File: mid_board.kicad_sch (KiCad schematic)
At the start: 21 parts, among them J4 Conn_01x10_Pin, J5 Conn_01x02_Pin, J6 Conn_01x11_Pin, J7 Conn_01x07_Pin, J8 Conn_01x08_Pin, J9 Conn_01x06_Pin, U2 Z80CPU, U3 74LS374, U4 74ALS00, U5 74ALS32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

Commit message: Added some basic traces for power
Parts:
- removed C1, C2, C3, C4, C5: C_Small, symbol Device:C_Small
- removed J4: Conn_01x10_Pin, symbol Connector:Conn_01x10_Pin
- removed J5: Conn_01x02_Pin, symbol Connector:Conn_01x02_Pin
- removed J6: Conn_01x11_Pin, symbol Connector:Conn_01x11_Pin
- removed J7: Conn_01x07_Pin, symbol Connector:Conn_01x07_Pin
- removed J8: Conn_01x08_Pin, symbol Connector:Conn_01x08_Pin
- removed J9: Conn_01x06_Pin, symbol Connector:Conn_01x06_Pin
- removed U8, U9: 74LS83, symbol 74xx:74LS83
- added U20, U8: 74LS283, Package_SO:SOIC-16_3.9x9.9mm_P1.27mm, symbol 74xx:74LS283
- R1, R2: footprint (none) -> Resistor_SMD:R_1206_3216Metric_Pad1.30x1.75mm_HandSolder
- U2: footprint (none) -> Package_DIP:DIP-40_W15.24mm_Socket
- U3, U6, U7: footprint (none) -> Package_SO:SO-20_5.3x12.6mm_P1.27mm
- U4, U5: footprint (none) -> Package_SO:SOIC-14_3.9x8.7mm_P1.27mm
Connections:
- net A0: now also U8.11 (B4)
- net A1: now also U20.11 (B4)
- net A2: now also U8.15 (B3)
- net A3: now also U20.15 (B3)
- net A4: now also U8.2 (B2)
- net A5: now also U20.2 (B2)
- net A6: now also U8.6 (B1)
- net A7: now also U20.6 (B1)
- net BUF_D0: now also U8.12 (A4)
- net BUF_D1: now also U8.14 (A3)
- net BUF_D2: now also U8.3 (A2)
- net BUF_D3: now also U8.5 (A1)
- net BUF_D4: now also U20.12 (A4)
- net BUF_D5: now also U20.14 (A3)
- net BUF_D6: now also U20.3 (A2)
- net BUF_D7: now also U20.5 (A1)
- net GND: now also U4.1, U4.12, U4.13, U4.2, U20.8 (GND), U8.7 (C0), U8.8 (GND)
- net VCC: now also U20.16 (VCC), U8.16 (VCC)
- net at U7.11 (I0b): now also U20.4 (S1)
- net at U7.13 (I1b): now also U20.1 (S2)
- net at U7.15 (I2b): now also U20.13 (S3)
- net at U7.17 (I3b): now also U20.10 (S4)
- net at U7.2 (I0a): now also U8.4 (S1)
- net at U7.4 (I1a): now also U8.1 (S2)
- net at U7.6 (I2a): now also U8.13 (S3)
- net at U7.8 (I3a): now also U8.10 (S4)
- new net: U20.7 (C0), U8.9 (C4)
- no-connect marks 7 -> 3
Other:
- moved on the sheet: U4E, U5E

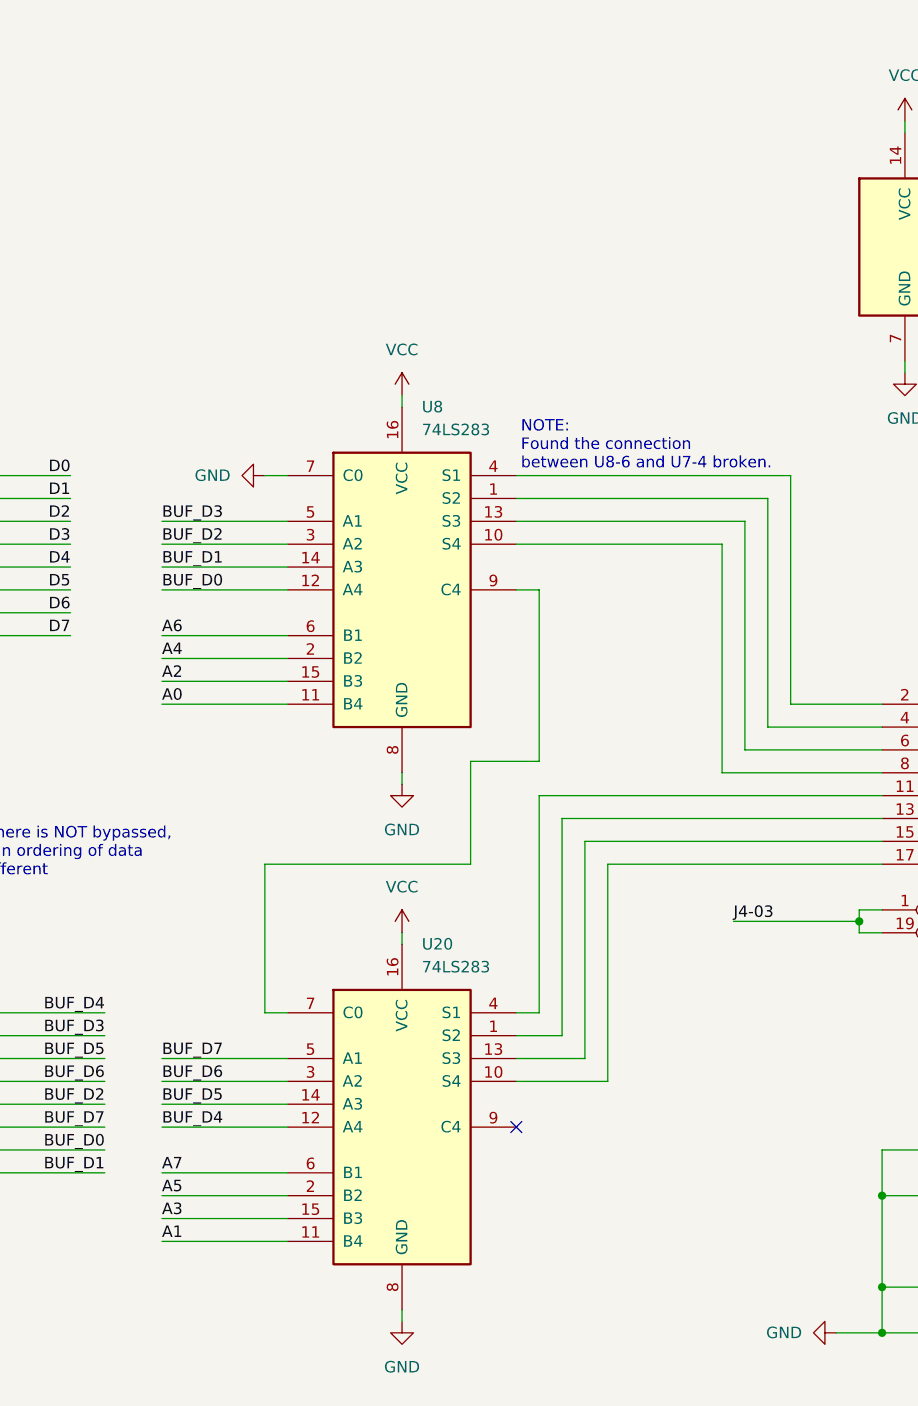
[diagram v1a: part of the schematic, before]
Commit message: Fix adder bit ordering
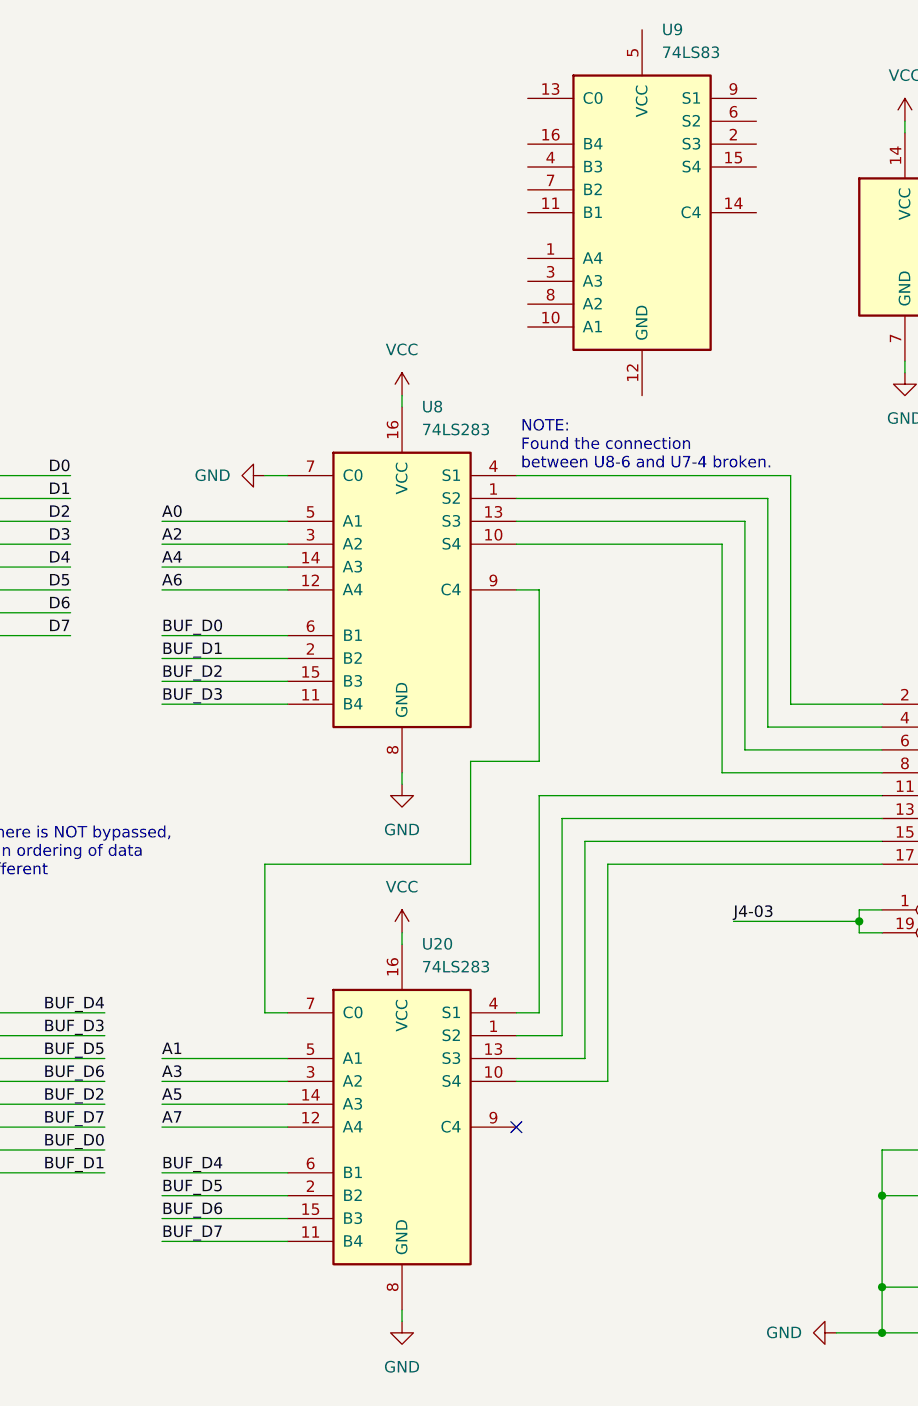
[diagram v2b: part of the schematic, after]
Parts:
- added U9: 74LS83, symbol 74xx:74LS83
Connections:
- net A0: now also U8.5 (A1); no longer U8.11 (B4)
- net A1: now also U20.5 (A1); no longer U20.11 (B4)
- net A2: now also U8.3 (A2); no longer U8.15 (B3)
- net A3: now also U20.3 (A2); no longer U20.15 (B3)
- net A4: now also U8.14 (A3); no longer U8.2 (B2)
- net A5: now also U20.14 (A3); no longer U20.2 (B2)
- net A6: now also U8.12 (A4); no longer U8.6 (B1)
- net A7: now also U20.12 (A4); no longer U20.6 (B1)
- net BUF_D0: now also U8.6 (B1); no longer U8.12 (A4)
- net BUF_D1: now also U8.2 (B2); no longer U8.14 (A3)
- net BUF_D2: now also U8.15 (B3); no longer U8.3 (A2)
- net BUF_D3: now also U8.11 (B4); no longer U8.5 (A1)
- net BUF_D4: now also U20.6 (B1); no longer U20.12 (A4)
- net BUF_D5: now also U20.2 (B2); no longer U20.14 (A3)
- net BUF_D6: now also U20.15 (B3); no longer U20.3 (A2)
- net BUF_D7: now also U20.11 (B4); no longer U20.5 (A1)
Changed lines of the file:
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@@
 	(wire
 		(pts
-			(xy 153.67 134.62) (xy 167.64 134.62)
+			(xy 153.67 144.78) (xy 167.64 144.78)
 		)
 		(stroke
@@
 	(wire
 		(pts
-			(xy 153.67 77.47) (xy 167.64 77.47)
+			(xy 153.67 82.55) (xy 167.64 82.55)
 		)
 		(stroke
@@
 	(wire
 		(pts
-			(xy 153.67 90.17) (xy 167.64 90.17)
+			(xy 153.67 69.85) (xy 167.64 69.85)
 		)
 		(stroke
@@
 	(wire
 		(pts
-			(xy 153.67 87.63) (xy 167.64 87.63)
+			(xy 153.67 72.39) (xy 167.64 72.39)
 		)
 		(stroke
@@
 	(wire
 		(pts
-			(xy 153.67 69.85) (xy 167.64 69.85)
+			(xy 153.67 90.17) (xy 167.64 90.17)
 		)
 		(stroke
@@
 	(wire
 		(pts
-			(xy 153.67 147.32) (xy 167.64 147.32)
+			(xy 153.67 132.08) (xy 167.64 132.08)
 		)
 		(stroke
@@
 	(wire
 		(pts
-			(xy 153.67 72.39) (xy 167.64 72.39)
+			(xy 153.67 87.63) (xy 167.64 87.63)
 		)
 		(stroke
@@
 	(wire
 		(pts
-			(xy 153.67 132.08) (xy 167.64 132.08)
+			(xy 153.67 147.32) (xy 167.64 147.32)
 		)
 		(stroke
@@
 	(wire
 		(pts
-			(xy 153.67 74.93) (xy 167.64 74.93)
+			(xy 153.67 85.09) (xy 167.64 85.09)
 		)
 		(stroke
@@
 	(wire
 		(pts
-			(xy 153.67 137.16) (xy 167.64 137.16)
+			(xy 153.67 142.24) (xy 167.64 142.24)
 		)
 		(stroke
@@
 	(wire
 		(pts
-			(xy 153.67 149.86) (xy 167.64 149.86)
+			(xy 153.67 129.54) (xy 167.64 129.54)
 		)
 		(stroke
@@
 	(wire
 		(pts
-			(xy 153.67 142.24) (xy 167.64 142.24)
+			(xy 153.67 137.16) (xy 167.64 137.16)
 		)
 		(stroke
@@
 	(wire
 		(pts
-			(xy 153.67 129.54) (xy 167.64 129.54)
+			(xy 153.67 149.86) (xy 167.64 149.86)
 		)
 		(stroke
@@
 	(wire
 		(pts
-			(xy 153.67 85.09) (xy 167.64 85.09)
+			(xy 153.67 74.93) (xy 167.64 74.93)
 		)
 		(stroke
@@
 	(wire
 		(pts
-			(xy 153.67 82.55) (xy 167.64 82.55)
+			(xy 153.67 77.47) (xy 167.64 77.47)
 		)
 		(stroke
@@
 	(wire
 		(pts
-			(xy 153.67 144.78) (xy 167.64 144.78)
+			(xy 153.67 134.62) (xy 167.64 134.62)
 		)
 		(stroke
@@
 	)
 	(label "BUF_D0"
-		(at 153.67 77.47 0)
+		(at 153.67 82.55 0)
 		(fields_autoplaced yes)
 		(effects
@@
 	)
 	(label "BUF_D7"
-		(at 153.67 129.54 0)
+		(at 153.67 149.86 0)
 		(fields_autoplaced yes)
 		(effects
@@
 	)
 	(label "BUF_D5"
-		(at 153.67 134.62 0)
+		(at 153.67 144.78 0)
 		(fields_autoplaced yes)
 		(effects
@@
 	)
 	(label "BUF_D4"
-		(at 153.67 137.16 0)
+		(at 153.67 142.24 0)
 		(fields_autoplaced yes)
 		(effects
@@
 	)
 	(label "A7"
-		(at 153.67 142.24 0)
+		(at 153.67 137.16 0)
 		(fields_autoplaced yes)
 		(effects
@@
 	)
 	(label "A2"
-		(at 153.67 87.63 0)
+		(at 153.67 72.39 0)
 		(fields_autoplaced yes)
 		(effects
@@
 	)
 	(label "A1"
-		(at 153.67 149.86 0)
+		(at 153.67 129.54 0)
 		(fields_autoplaced yes)
 		(effects
@@
 	)
 	(label "BUF_D2"
-		(at 153.67 72.39 0)
+		(at 153.67 87.63 0)
 		(fields_autoplaced yes)
 		(effects
@@
 	)
 	(label "A5"
-		(at 153.67 144.78 0)
+		(at 153.67 134.62 0)
 		(fields_autoplaced yes)
 		(effects
@@
 	)
 	(label "A0"
-		(at 153.67 90.17 0)
+		(at 153.67 69.85 0)
 		(fields_autoplaced yes)
 		(effects
@@
 	)
 	(label "A4"
-		(at 153.67 85.09 0)
+		(at 153.67 74.93 0)
 		(fields_autoplaced yes)
 		(effects
@@
 	)
 	(label "BUF_D1"
-		(at 153.67 74.93 0)
+		(at 153.67 85.09 0)
 		(fields_autoplaced yes)
 		(effects
@@
 	)
 	(label "BUF_D6"
-		(at 153.67 132.08 0)
+		(at 153.67 147.32 0)
 		(fields_autoplaced yes)
 		(effects
@@
 	)
 	(label "A6"
-		(at 153.67 82.55 0)
+		(at 153.67 77.47 0)
 		(fields_autoplaced yes)
 		(effects
@@
 	)
 	(label "BUF_D3"
-		(at 153.67 69.85 0)
+		(at 153.67 90.17 0)
 		(fields_autoplaced yes)
 		(effects
@@
 	)
 	(label "A3"
-		(at 153.67 147.32 0)
+		(at 153.67 132.08 0)
 		(fields_autoplaced yes)
 		(effects
@@
 					(unit 1)
 				)
+			)
+		)
+	)
+	(symbol
+		(lib_id "74xx:74LS83")
+		(at 207.01 35.56 0)
+		(unit 1)
+		(exclude_from_sim no)
+		(in_bom yes)
+		(on_board yes)
+		(dnp no)
+		(fields_autoplaced yes)
+		(property "Reference" "U9"
+			(at 209.2041 15.24 0)
+			(effects
+				(font
+					(size 1.27 1.27)
+				)
+				(justify left)
+			)
+		)
+		(property "Value" "74LS83"
+			(at 209.2041 17.78 0)
+			(effects
+				(font
+					(size 1.27 1.27)
+				)
+				(justify left)
+			)
+		)
+		(property "Footprint" ""
+			(at 207.01 35.56 0)
+			(effects
+				(font
+					(size 1.27 1.27)
+				)
+				(hide yes)
+			)
+		)
+		(property "Datasheet" "http://www.ti.com/lit/gpn/sn74LS83"
+			(at 207.01 35.56 0)
+			(effects
+				(font
+					(size 1.27 1.27)
+				)
+				(hide yes)
+			)
+		)
+		(property "Description" "4-bit Full Adder"
+			(at 207.01 35.56 0)
+			(effects
+				(font
+					(size 1.27 1.27)
+				)
+				(hide yes)
+			)
+		)
+		(pin "11"
+		)
+		(pin "13"
+		)
+		(pin "16"
+		)
+		(pin "14"
+		)
+		(pin "9"
+		)
+		(pin "10"
+		)
+		(pin "12"
+		)
+		(pin "15"
+		)
+		(pin "2"
+		)
+		(pin "5"
+		)
+		(pin "6"
+		)
+		(pin "7"
+		)
+		(pin "1"
+		)
+		(pin "4"
+		)
+		(pin "3"
+		)
+		(pin "8"
+		)
+		(instances
+			(project ""
+				(path "/6f5335a8-66b5-468f-92d4-becfba378f22/b0dc1deb-a268-4097-a7cc-08028e687e23/0ce60583-d30f-4b91-b1c6-5cebb37feada"
+					(reference "U9")
+					(unit 1)
+				)

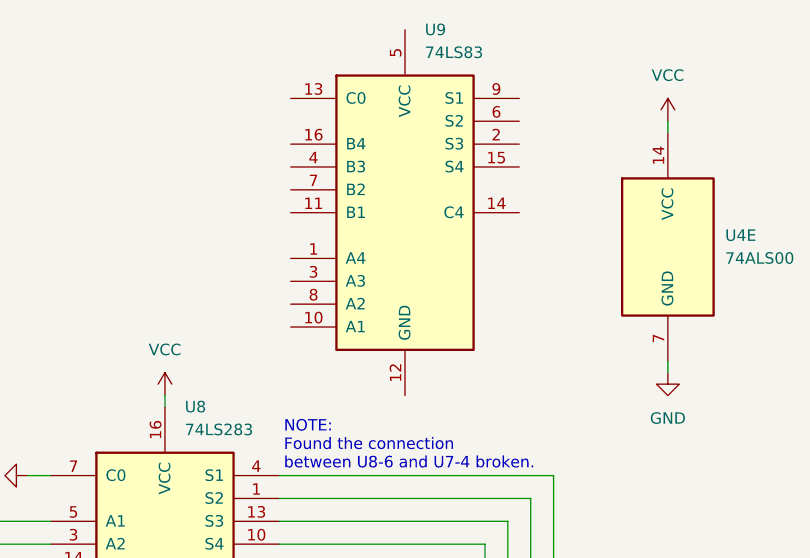
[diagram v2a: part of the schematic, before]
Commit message: Update board fixing adder issues
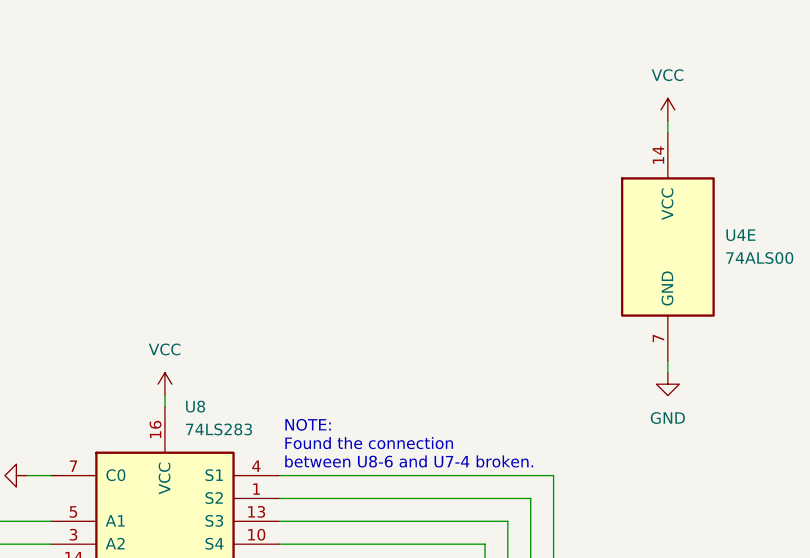
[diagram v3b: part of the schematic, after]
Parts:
- removed U9: 74LS83, symbol 74xx:74LS83
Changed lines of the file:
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@@
-	)
-	(symbol
-		(lib_id "74xx:74LS83")
-		(at 207.01 35.56 0)
-		(unit 1)
-		(exclude_from_sim no)
-		(in_bom yes)
-		(on_board yes)
-		(dnp no)
-		(fields_autoplaced yes)
-		(property "Reference" "U9"
-			(at 209.2041 15.24 0)
-			(effects
-				(font
-					(size 1.27 1.27)
-				)
-				(justify left)
-			)
-		)
-		(property "Value" "74LS83"
-			(at 209.2041 17.78 0)
-			(effects
-				(font
-					(size 1.27 1.27)
-				)
-				(justify left)
-			)
-		)
-		(property "Footprint" ""
-			(at 207.01 35.56 0)
-			(effects
-				(font
-					(size 1.27 1.27)
-				)
-				(hide yes)
-			)
-		)
-		(property "Datasheet" "http://www.ti.com/lit/gpn/sn74LS83"
-			(at 207.01 35.56 0)
-			(effects
-				(font
-					(size 1.27 1.27)
-				)
-				(hide yes)
-			)
-		)
-		(property "Description" "4-bit Full Adder"
-			(at 207.01 35.56 0)
-			(effects
-				(font
-					(size 1.27 1.27)
-				)
-				(hide yes)
-			)
-		)
-		(pin "11"
-		)
-		(pin "13"
-		)
-		(pin "16"
-		)
-		(pin "14"
-		)
-		(pin "9"
-		)
-		(pin "10"
-		)
-		(pin "12"
-		)
-		(pin "15"
-		)
-		(pin "2"
-		)
-		(pin "5"
-		)
-		(pin "6"
-		)
-		(pin "7"
-		)
-		(pin "1"
-		)
-		(pin "4"
-		)
-		(pin "3"
-		)
-		(pin "8"
-		)
-		(instances
-			(project ""
-				(path "/6f5335a8-66b5-468f-92d4-becfba378f22/b0dc1deb-a268-4097-a7cc-08028e687e23/0ce60583-d30f-4b91-b1c6-5cebb37feada"
-					(reference "U9")
-					(unit 1)
-				)
-			)
-		)
 	)
 	(symbol

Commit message: Removed some text from schematic, added some more, generate PDF
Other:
- note added: "The original board used 74LS83s, that are almost impossible to find. Replaced with functionally similar '283."
- note removed: "NOTE: Found the connection between U8-6 and U7-4 broken."
- note removed: "Some input pins are swapped here, still functionally identical"
- note removed: "The '245 here is NOT bypassed, and the pin ordering of data lines is different"
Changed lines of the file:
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@@
 		)
 	)
-	(text "The '245 here is NOT bypassed,\nand the pin ordering of data\nlines is different"
+	(text "The original board used\n74LS83s, that are almost\nimpossible to find.\n\nReplaced with functionally \nsimilar '283."
 		(exclude_from_sim no)
-		(at 127 106.68 0)
+		(at 194.31 55.372 0)
 		(effects
 			(font
-				(size 1.27 1.27)
-			)
-			(justify left)
-		)
-	)
-	(text "Some input pins are swapped here,\nstill functionally identical"
-		(exclude_from_sim no)
-		(at 44.45 151.892 0)
-		(effects
-			(font
-				(size 1.27 1.27)
-			)
-			(justify left)
-		)
-	)
-	(text "NOTE:\nFound the connection\nbetween U8-6 and U7-4 broken.\n"
-		(exclude_from_sim no)
-		(at 193.548 61.468 0)
-		(effects
-			(font
